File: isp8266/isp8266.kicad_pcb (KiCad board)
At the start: 2 copper layers, 60 x 35 mm, 65 parts, among them J1 Bottom, J10 BAT2, J11 USB_C_Receptacle_USB2.0, J12 F1, J2 Up, J7 F0, J8 BAT1, Q1 S8050, Q2 S8050, Q3 BSS138, Q4 IRLML6402, Q5 BSS138, Q6 IRLML6402, U1 CH340C, U2 AP1117-33, U3 IP5306, U4 ESP-07

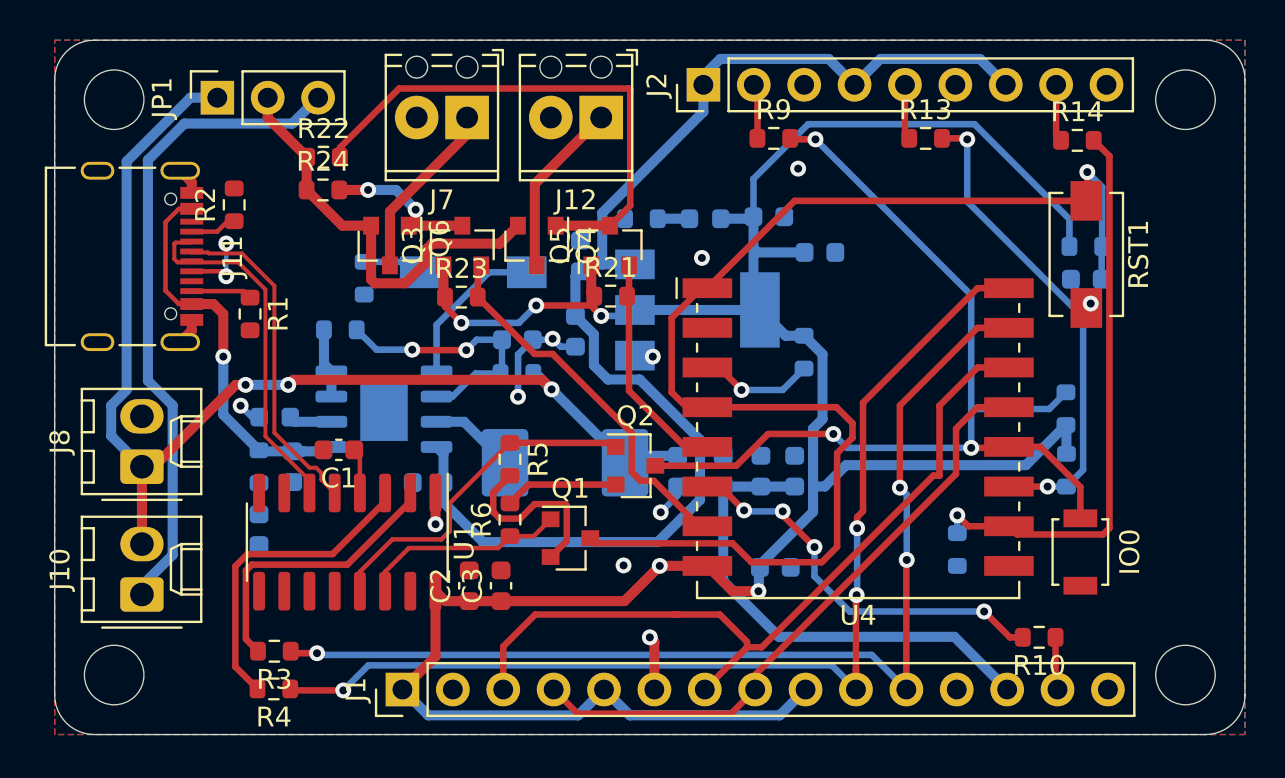
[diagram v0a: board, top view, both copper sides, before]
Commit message: Text and some routing
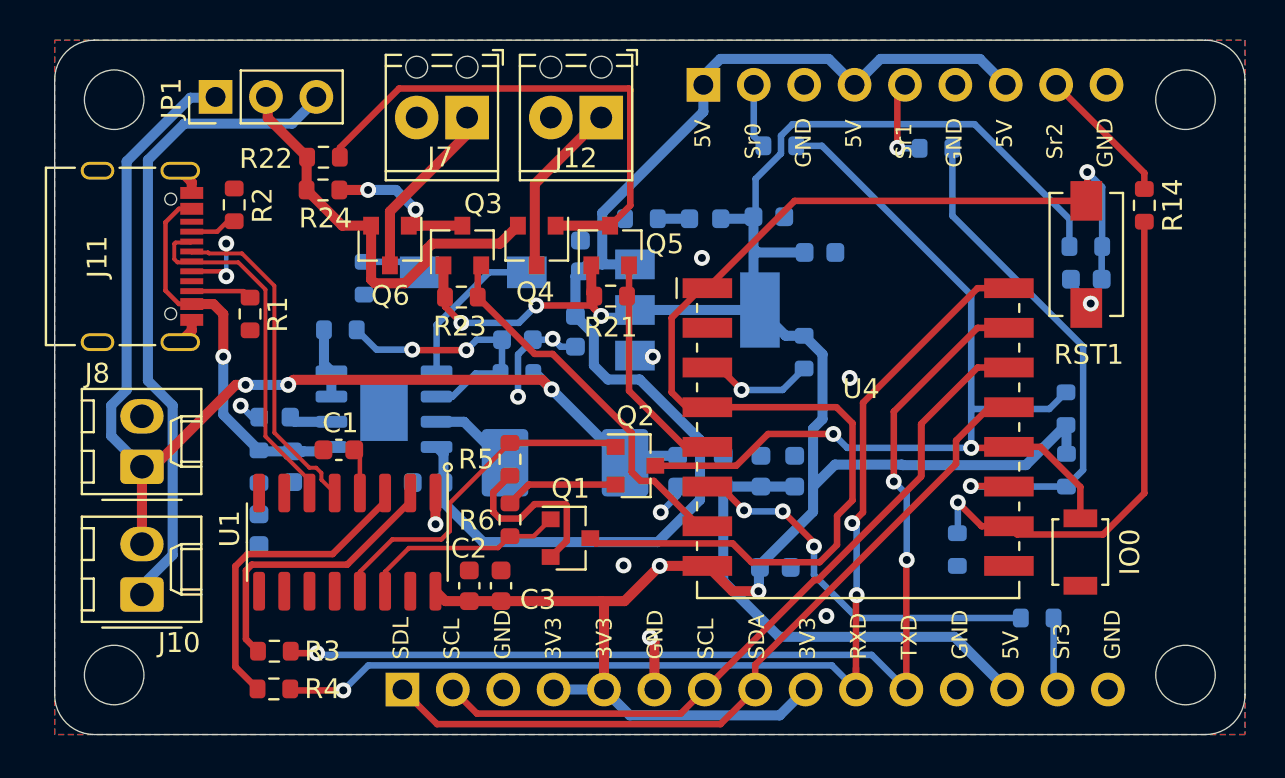
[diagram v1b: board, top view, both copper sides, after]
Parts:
- J1, J2, R10, R13, R9: moved to B.Cu
- JP1: footprint Connector_PinSocket_2.54mm:PinSocket_1x03_P2.54mm_Vertical -> Connector_PinHeader_2.54mm:PinHeader_1x03_P2.54mm_Vertical
- moved R14 4.70 mm to (91.9, 28.8), turned to 270 degrees
- moved R10 0.98 mm to (86.5, 49.6)
- moved R13 0.72 mm to (81.4, 25.9)
- moved R9 0.48 mm to (73.5, 25.8)
- moved JP1 0.10 mm to (45.1, 23.4)
- turned J1 to 270 degrees
- turned J2 to 270 degrees
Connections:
- J1 pad 1: +3V3 -> SDA
- J1 pad 2: -BATT -> SCL
- J1 pad 3: SCL -> -BATT
- J1 pad 4: SDA -> +3V3
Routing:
- net +3V3: track 132.1 -> 122.8 mm
- net SDA: track 31.6 -> 39.3 mm
- net Net-(J2-Pad8): track 2.90 -> 7.09 mm
- net GPIO15: track 29.0 -> 26.2 mm
- net IO2: track 24.5 -> 26.9 mm, vias 2 -> 1
- net Net-(J2-Pad5): track 2.79 -> 4.47 mm, vias 0 -> 1
- net Net-(J1-Pad14): track 2.67 -> 3.69 mm
- net GPIO12: track 20.0 -> 19.5 mm, vias 4 -> 3
- net IO0: track 50.1 -> 49.6 mm, vias 3 -> 2
- net -BATT: vias 11 -> 12
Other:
- board text added: "3V3"
- board text added: "5V"
- board text added: "GND"
- board text added: "RXD"
- board text added: "SCL"
- board text added: "SDA"
- board text added: "SDL"
- board text added: "Sr0"
- board text added: "Sr1"
- board text added: "Sr2"
- board text added: "Sr3"
- board text added: "TXD"

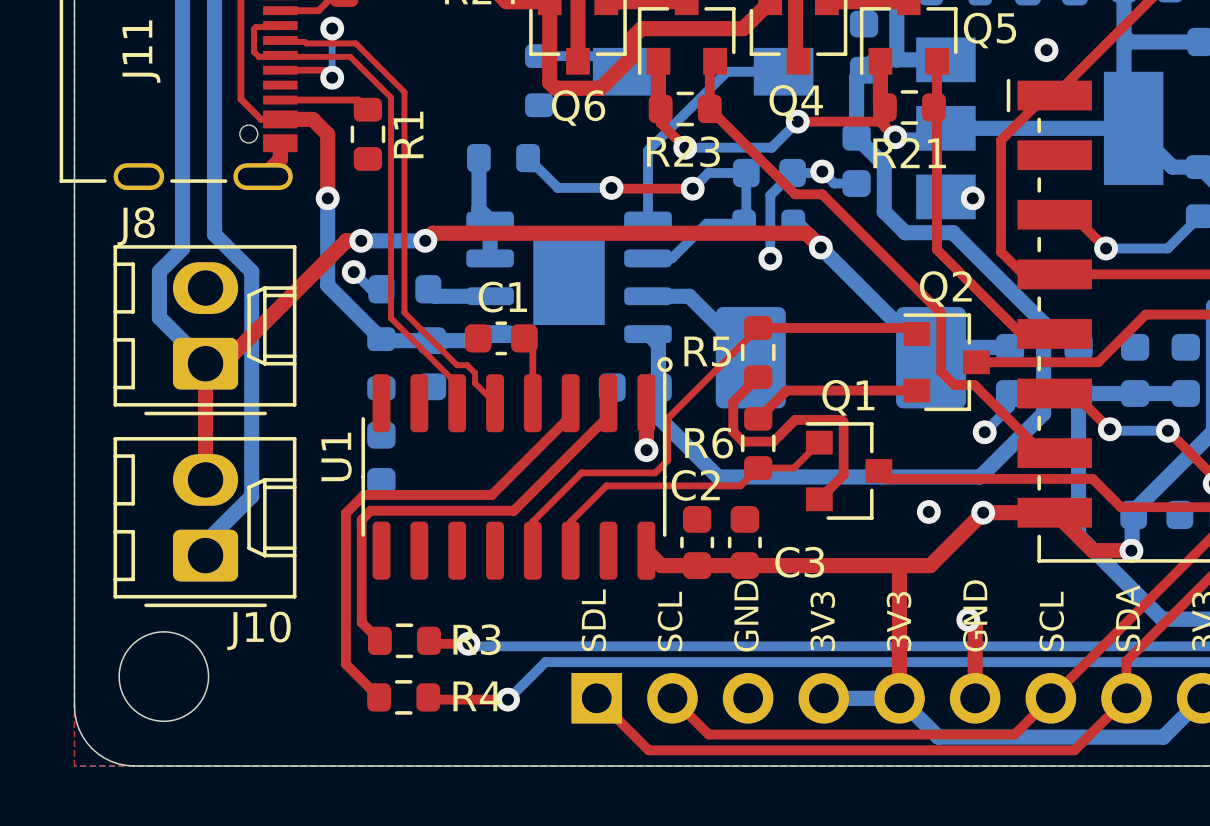
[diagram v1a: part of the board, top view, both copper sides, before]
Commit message: Add text and logo
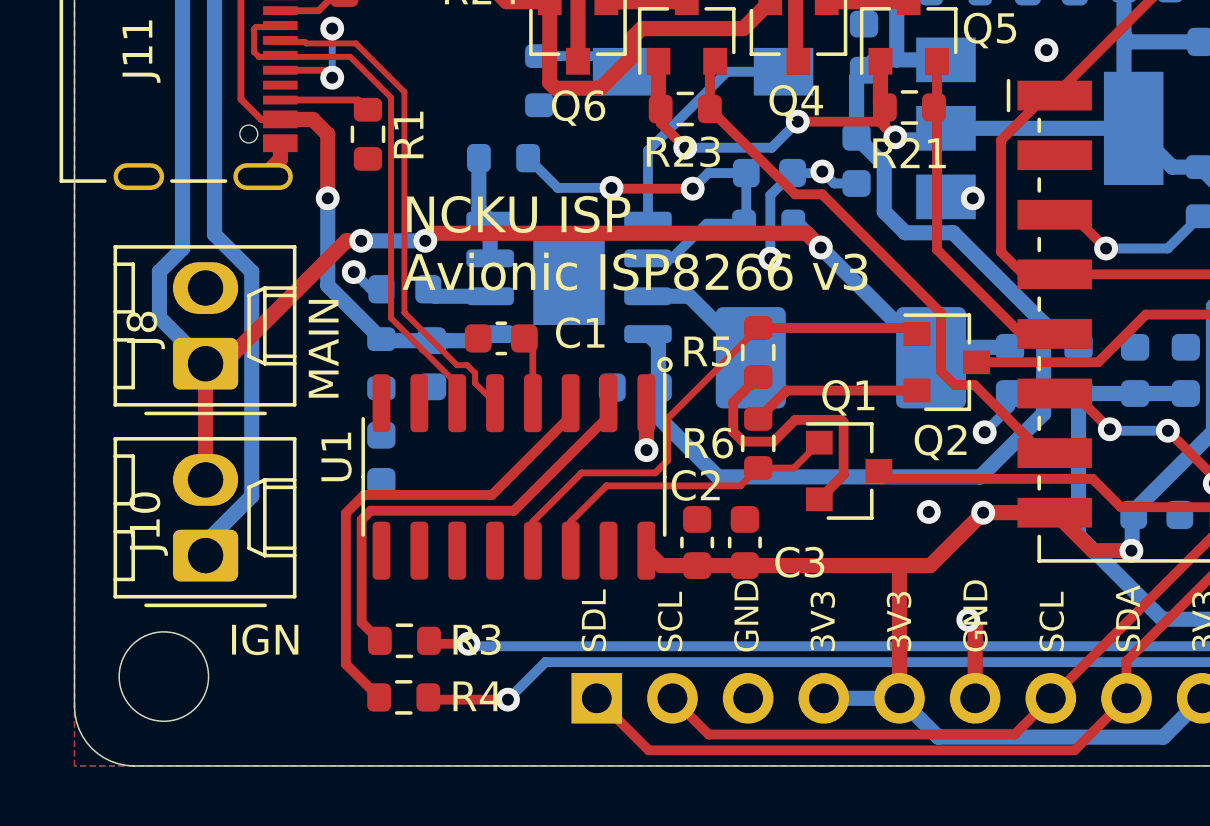
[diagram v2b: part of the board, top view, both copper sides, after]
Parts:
- added REF**: WEEE-Logo_4.2x6mm_SilkScreen, Symbol:WEEE-Logo_4.2x6mm_SilkScreen, B.Cu at (46.0, 51.0)
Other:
- board text added: "IGN"
- board text added: "MAIN"
- board text added: "NCKU ISP Avionic ISP8266 v3"

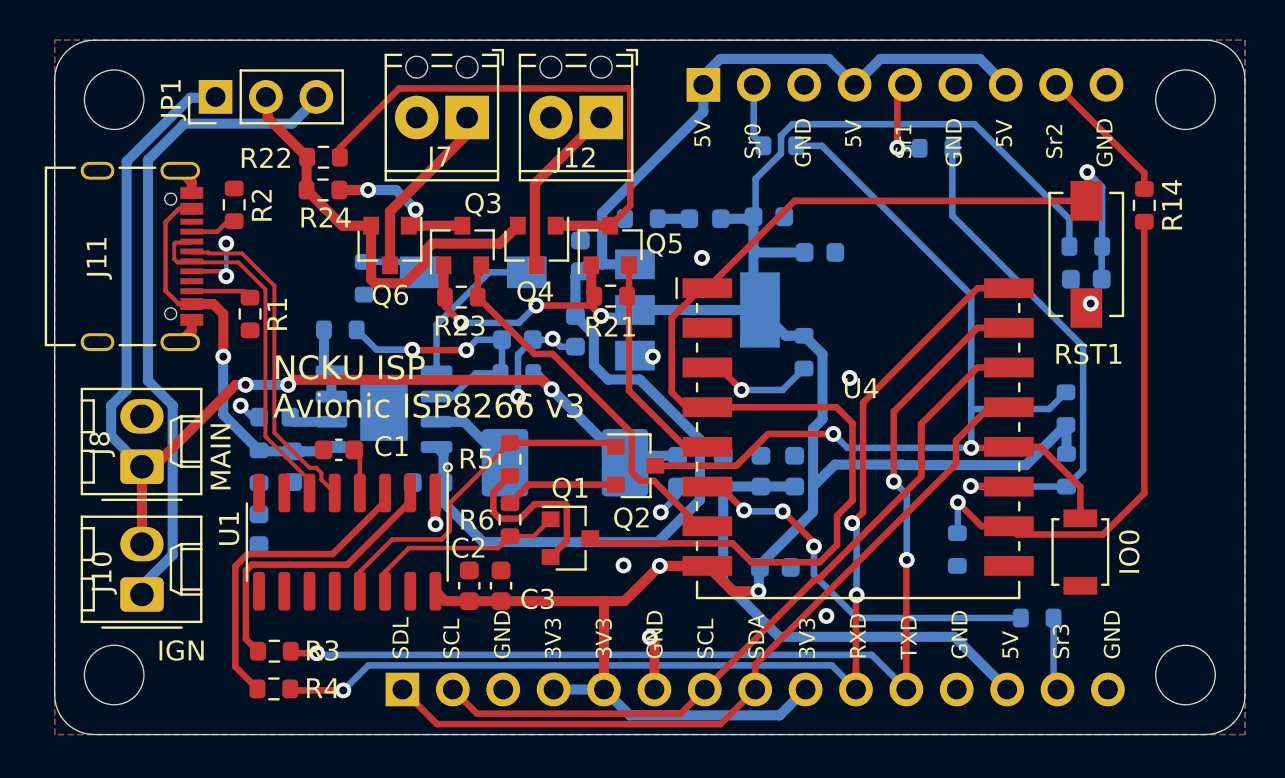
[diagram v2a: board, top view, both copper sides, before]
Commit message: Change switch position and battery connector
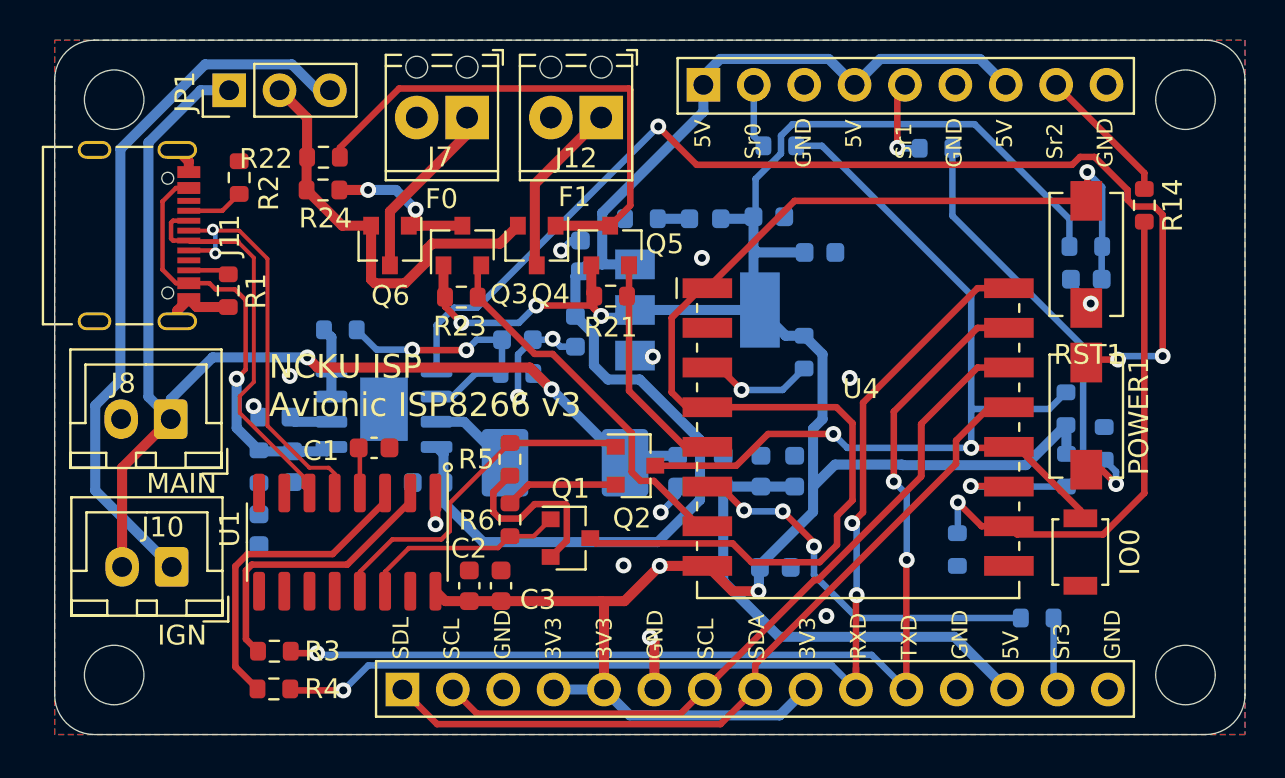
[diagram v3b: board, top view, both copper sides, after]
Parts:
- J10, J8: footprint Connector_Molex:Molex_KK-254_AE-6410-02A_1x02_P2.54mm_Vertical -> Connector_JST:JST_XH_B2B-XH-A_1x02_P2.50mm_Vertical
- POWER1: moved to F.Cu
- moved R12 38.2 mm to (89.9, 40.8), turned to 90 degrees
- moved POWER1 31.7 mm to (89.0, 39.5), turned to 270 degrees
- moved J8 2.80 mm to (42.9, 39.6), turned to 180 degrees
- moved J10 2.05 mm to (42.9, 47.0), turned to 180 degrees
- moved C1 1.78 mm to (53.1, 41.0), turned to 0 degrees
- moved R1 1.61 mm to (45.8, 33.1)
- moved R2 1.40 mm to (46.3, 27.4)
- moved J11 1.06 mm to (41.2, 30.4)
- moved JP1 0.76 mm to (45.8, 23.0)
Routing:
- net Net-(POWER1-Pad1): track 7.99 -> 56.7 mm, vias 0 -> 3
- net D-: track 18.1 -> 22.5 mm
- net +9V: track 32.9 -> 36.1 mm
- net -BATT: track 17.0 -> 19.8 mm, vias 12 -> 14
- net VBUS: track 20.4 -> 22.4 mm
- net Net-(J11-PadB5): track 3.07 -> 2.07 mm
- net +BATT: track 58.2 -> 59.1 mm, vias 3 -> 2
- net IO0: track 49.6 -> 48.9 mm
- net Net-(J11-PadA5): track 2.36 -> 2.89 mm
- net Net-(POWER1-Pad2): track 3.02 -> 3.27 mm, vias 0 -> 1
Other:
- board text added: "F0"
- board text added: "F1"

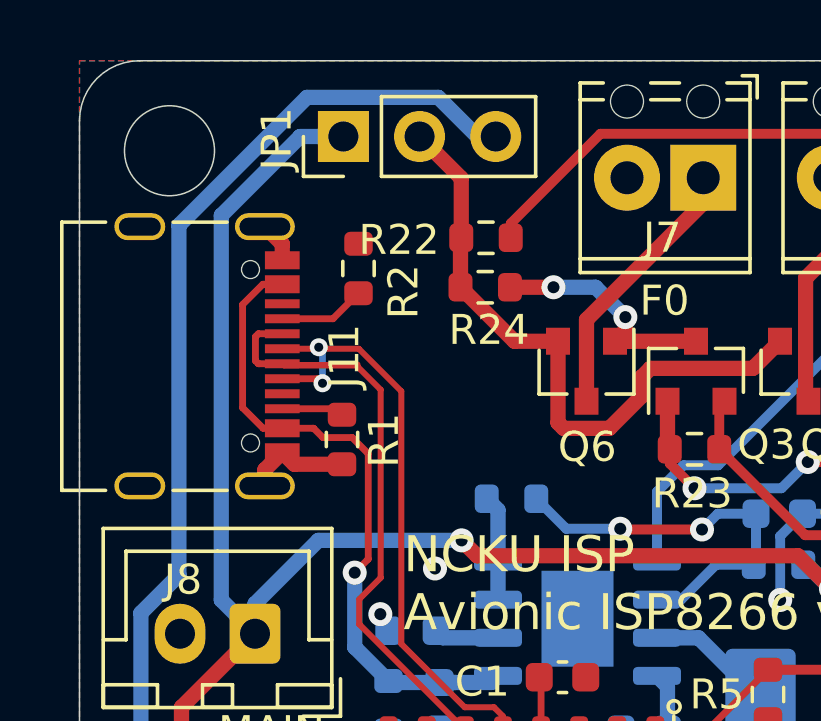
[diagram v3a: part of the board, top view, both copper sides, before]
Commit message: Add isp logo footprint
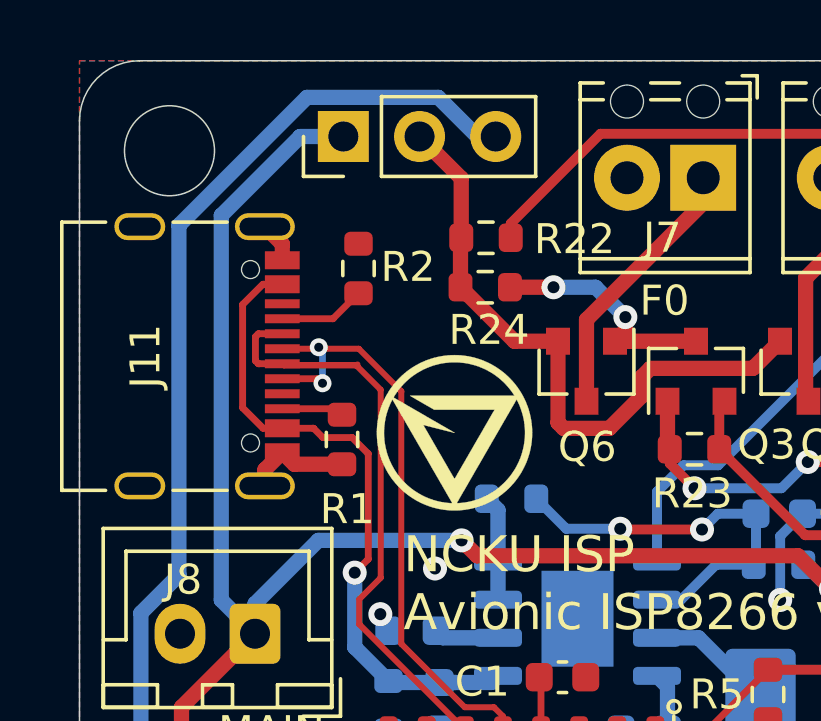
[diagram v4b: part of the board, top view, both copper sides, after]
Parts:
- added G***: LOGO, isp_logo:isp_logo, F.Cu at (49.5, 32.9)

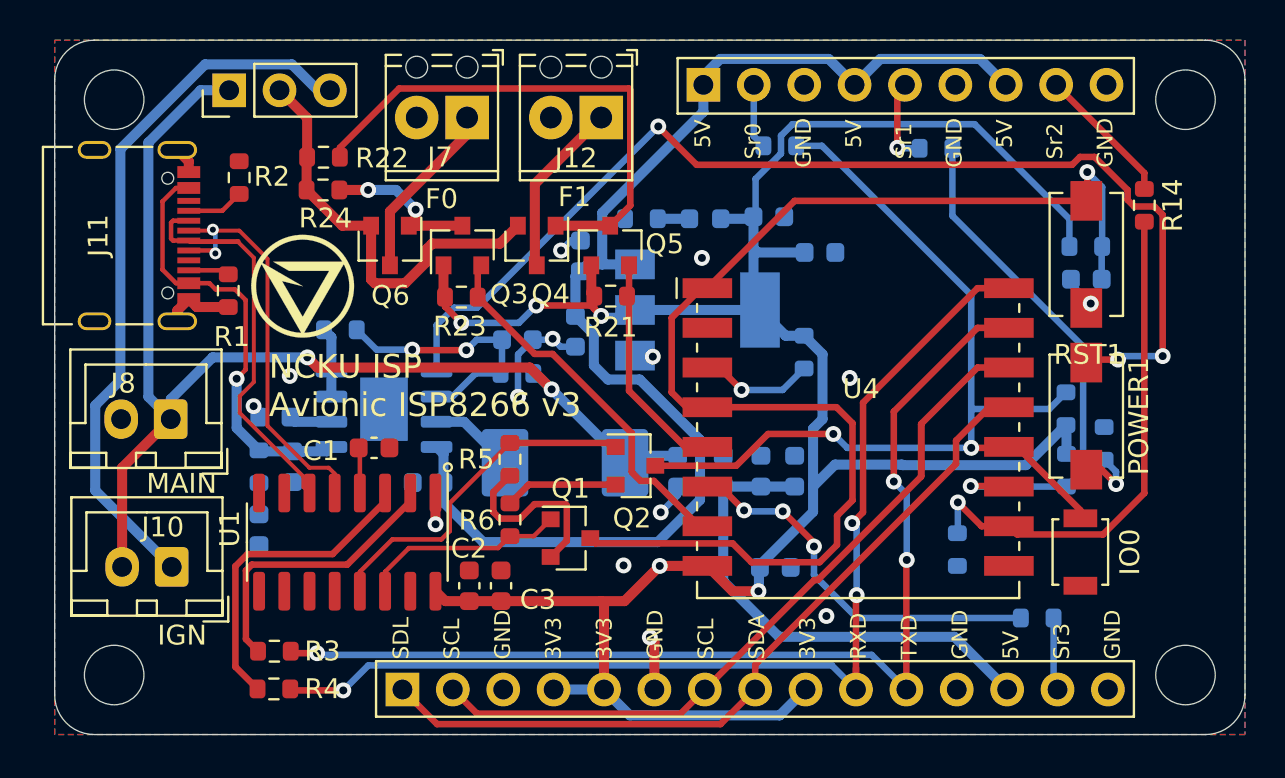
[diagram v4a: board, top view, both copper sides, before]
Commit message: Modify symbol location
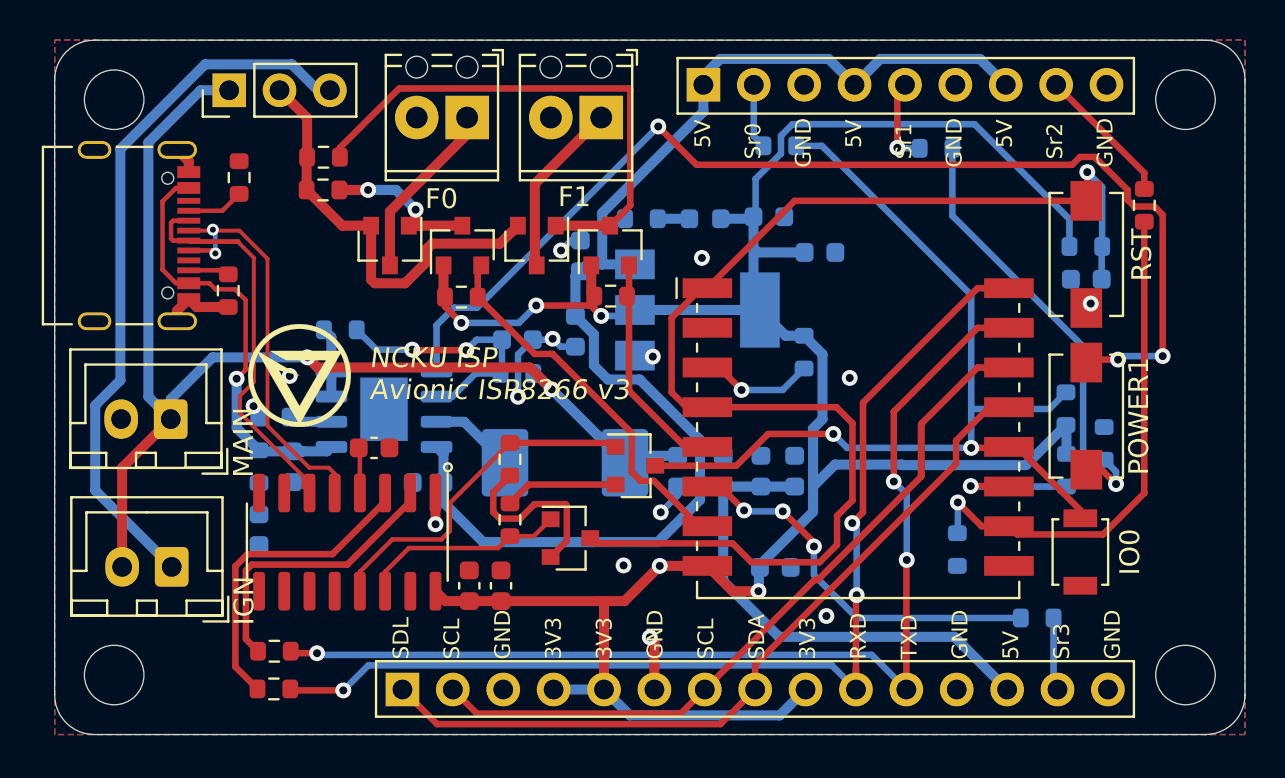
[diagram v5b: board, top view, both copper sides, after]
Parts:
- added REF**: OSHW-Logo_5.7x6mm_SilkScreen, Symbol:OSHW-Logo_5.7x6mm_SilkScreen, B.Cu at (56.1, 47.7)
- moved REF** 5.75 mm to (50.8, 47.8)
- moved G*** 4.50 mm to (49.3, 37.4)
- renumbered RST1 to RST
